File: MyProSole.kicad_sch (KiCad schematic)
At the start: 22 parts, among them J1 FSR3, J2 FSR2, J3 FSR3, J4 Conn_01x07_Socket_XIAO_ESP32C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, J5 i2c-bus, J6 SD_CardSocket, J7 XIAO_ESP32C3, J8 SD_CardSocketDummy

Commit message: Version 1.1
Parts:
- added F1: BAT_FUSED, Fuse:Fuse_1206_3216Metric_Pad1.42x1.75mm_HandSolder, symbol Device:Fuse_Small
- added J9: BAT_RAW, Connector_JST:JST_PH_B2B-PH-K_1x02_P2.00mm_Vertical, symbol Connector_Generic:Conn_01x02
- added SW1: SW_SPDT, MyProSoleLibrary:WS-SLTU THT Mini Slide Switch, symbol Switch:SW_SPDT
- added TP2, TP3: TestPoint, TestPoint:TestPoint_Pad_2.0x2.0mm, symbol Connector:TestPoint
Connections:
- new net: SW1.3 (C), TP2.1
- new net: F1.1, J9.2 (Pin_2)
- new net: F1.2, SW1.2 (B)
- new net: J9.1 (Pin_1), TP3.1
- no-connect marks 7 -> 8

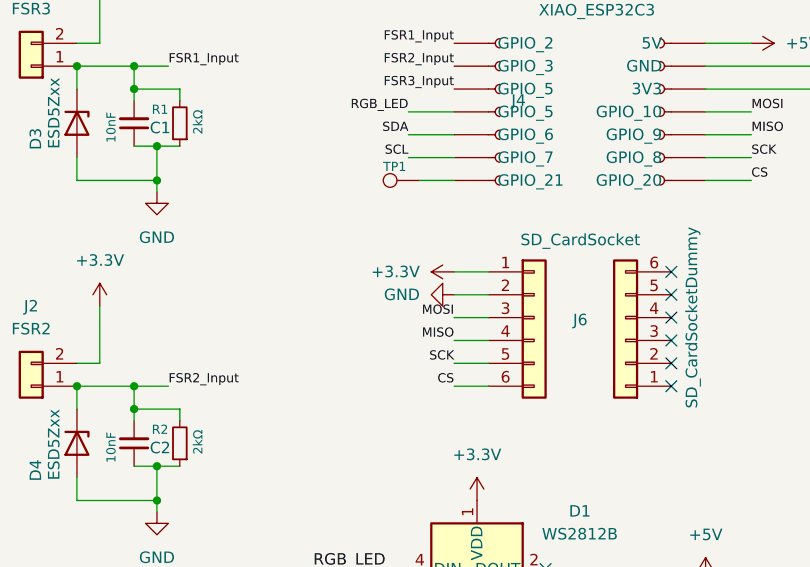
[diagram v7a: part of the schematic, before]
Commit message: Swap SD Card GND and 3V3
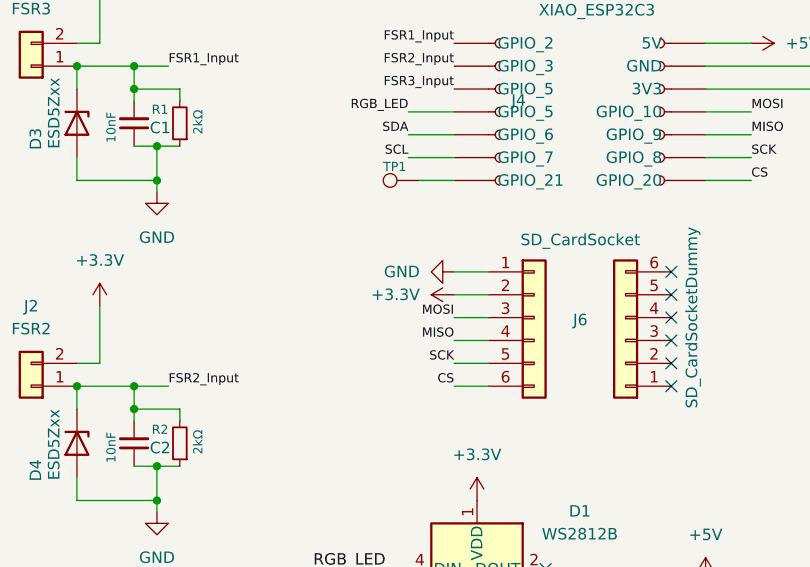
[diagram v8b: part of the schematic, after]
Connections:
- net +3.3V: now also J6.2 (Pin_2); no longer J6.1 (Pin_1)
- net GND: now also J6.1 (Pin_1); no longer J6.2 (Pin_2)
